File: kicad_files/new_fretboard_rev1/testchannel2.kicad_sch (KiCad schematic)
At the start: 22 parts, among them U2 LX3302AQPW-TR-EASY

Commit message: version with three coil circuits, some errors
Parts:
- removed C12, C13: 680pf, Capacitor_SMD:C_0603_1608Metric, symbol Device:C
- removed C14, C15: 10pf, Capacitor_SMD:C_0402_1005Metric, symbol Device:C
- removed C16: 1uf, Capacitor_SMD:C_0603_1608Metric, symbol Device:C
- removed C17, C20: 100nf, Capacitor_SMD:C_0402_1005Metric, symbol Device:C
- removed C18, C19: 6.8nf, Capacitor_SMD:C_0402_1005Metric, symbol Device:C
- removed C21: 1000pf, Capacitor_SMD:C_0402_1005Metric, symbol Device:C
- removed C22: 470nf, Capacitor_SMD:C_0402_1005Metric, symbol Device:C
- removed L5, L6, L7, L8: L, NetTie:NetTie-2_SMD_Pad0.5mm, symbol Device:L
- removed R10, R11, R8, R9: 10R, Resistor_SMD:R_0402_1005Metric, symbol Device:R
- removed R12: 221R, Resistor_SMD:R_0402_1005Metric, symbol Device:R
- removed R13: 4.7R, Resistor_SMD:R_0402_1005Metric, symbol Device:R
- removed U2: LX3302AQPW-TR-EASY, Snapeda:14-TSSOP_MCH-L, symbol Snapeda:LX3302AQPW-TR-EASY
- added C23, C29: 100nf, Capacitor_SMD:C_0402_1005Metric, symbol Device:C
- added C24: 1000pf, Capacitor_SMD:C_0402_1005Metric, symbol Device:C
- added C25: 470nf, Capacitor_SMD:C_0402_1005Metric, symbol Device:C
- added C26: 1uf, Capacitor_SMD:C_0603_1608Metric, symbol Device:C
- added C27, C28: 6.8nf, Capacitor_SMD:C_0402_1005Metric, symbol Device:C
- added C30, C31: 10pf, Capacitor_SMD:C_0402_1005Metric, symbol Device:C
- added C32, C33: 680pf, Capacitor_SMD:C_0603_1608Metric, symbol Device:C
- added L10, L11, L12, L9: L, NetTie:NetTie-2_SMD_Pad0.5mm, symbol Device:L
- added R14: 221R, Resistor_SMD:R_0402_1005Metric, symbol Device:R
- added R15, R16, R17, R18: 10R, Resistor_SMD:R_0402_1005Metric, symbol Device:R
- added R7: 4.7R, Resistor_SMD:R_0402_1005Metric, symbol Device:R
- added U3: LX3302AQPW-TR-EASY, Snapeda:14-TSSOP_MCH-L, symbol Snapeda:LX3302AQPW-TR-EASY
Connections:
- net CL1B_A: now also L12.1, R18.2
- net CL1_A: now also C30.1, R18.1, U3.8 (CL1)
- net CL2B_A: now also L11.1, R17.2
- net CL2_A: now also C31.1, R17.1, U3.10 (CL2)
- net GND: now also C23.1, C24.1, C25.1, C26.1, C27.1, C28.1, C30.2, C31.2, C32.2, C33.2, L11.2, L12.2, U3.2 (GND), U3.9 (GNDCL)
- net OSC11_A: now also C32.1, L9.2, U3.13 (OSC1)
- net OSC12_A: now also C33.1, L10.2, U3.12 (OSC2)
- net SUB_A: now also C29.1, U3.11 (SUB)
- net VIN_A: now also C24.2, C25.2, R15.2, R16.1, R7.1, U3.4 (VIN)
- new net: C26.2, C29.2, U3.5 (VDD)
- new net: C23.2, R7.2
- new net: C28.2, R14.1, R15.1, U3.6 (IO2)
- new net: C27.2, R14.2
- new net /OSC2B_A: L10.1, L9.1, R16.2
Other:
- removed sheet testchannel1
- removed sheet testchannel2

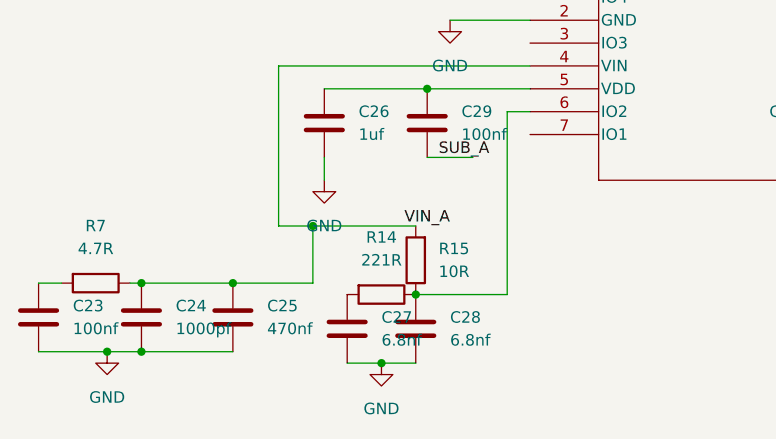
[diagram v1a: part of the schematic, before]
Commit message: stm32 micro added
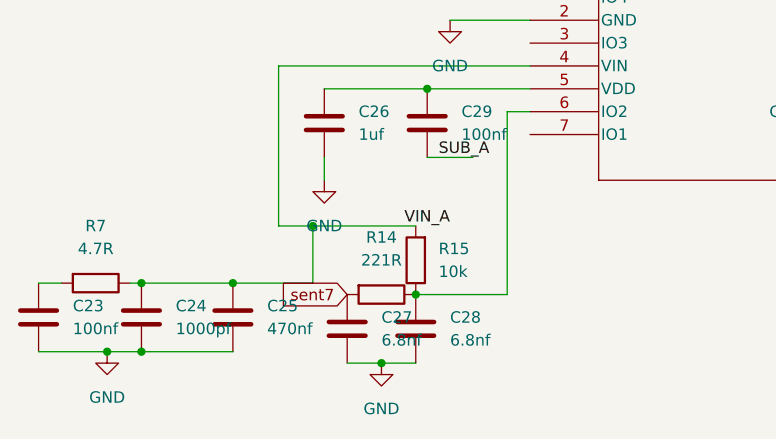
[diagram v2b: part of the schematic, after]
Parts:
- R15: value 10R -> 10k
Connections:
- net sent7: now reaches C27.2, R14.2

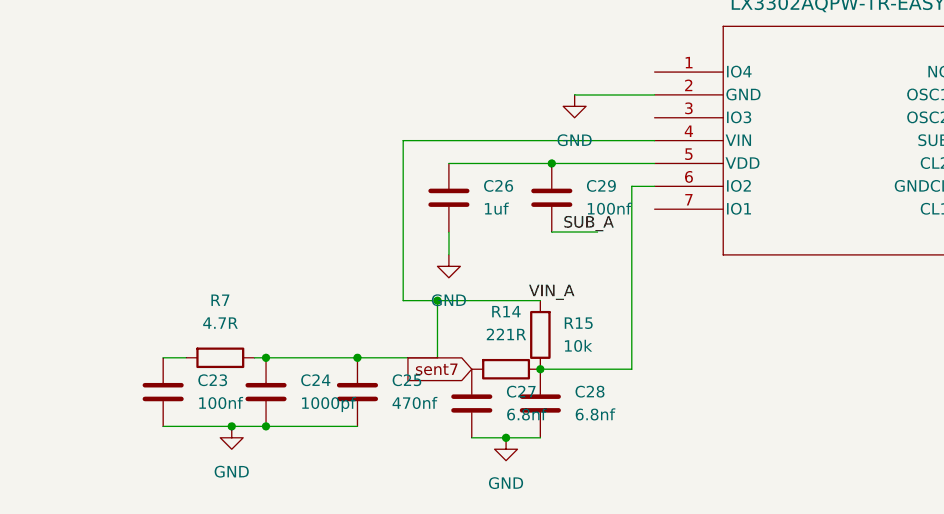
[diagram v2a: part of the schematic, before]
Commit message: mcu configured, still needs power connections and spi i2c connections
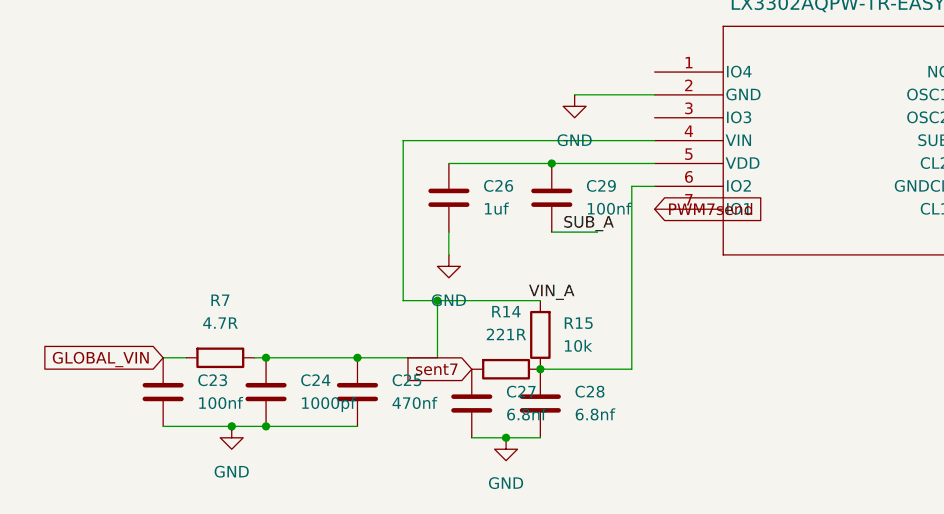
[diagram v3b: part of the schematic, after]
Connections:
- net GLOBAL_VIN: now reaches C23.2, R7.2
- net PWM7send: now reaches U3.7 (IO1)
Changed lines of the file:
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@@
+		)
+	)
+	(global_label "PWM7send"
+		(shape input)
+		(at 97.79 102.87 0)
+		(fields_autoplaced yes)
+		(effects
+			(font
+				(size 1.27 1.27)
+			)
+			(justify left)
+		)
+		(property "Intersheetrefs" "${INTERSHEET_REFS}"
+			(at 110.5722 102.87 0)
+			(effects
+				(font
+					(size 1.27 1.27)
+				)
+				(justify left)
+				(hide yes)
+			)
+		)
+	)
+	(global_label "GLOBAL_VIN"
+		(shape input)
+		(at 43.18 119.38 180)
+		(fields_autoplaced yes)
+		(effects
+			(font
+				(size 1.27 1.27)
+			)
+			(justify right)
+		)
+		(property "Intersheetrefs" "${INTERSHEET_REFS}"
+			(at 29.188 119.38 0)
+			(effects
+				(font
+					(size 1.27 1.27)
+				)
+				(justify right)
+				(hide yes)
+			)
 		)
 	)

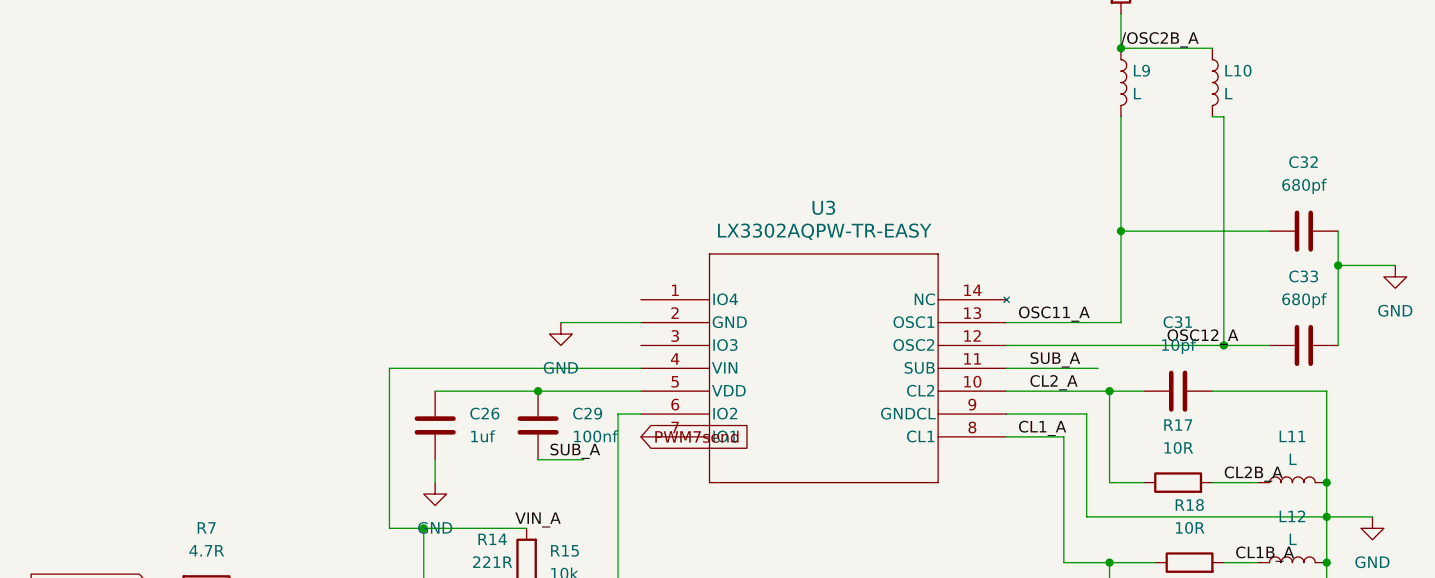
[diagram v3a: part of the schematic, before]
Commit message: finished routing - adding silkscreen
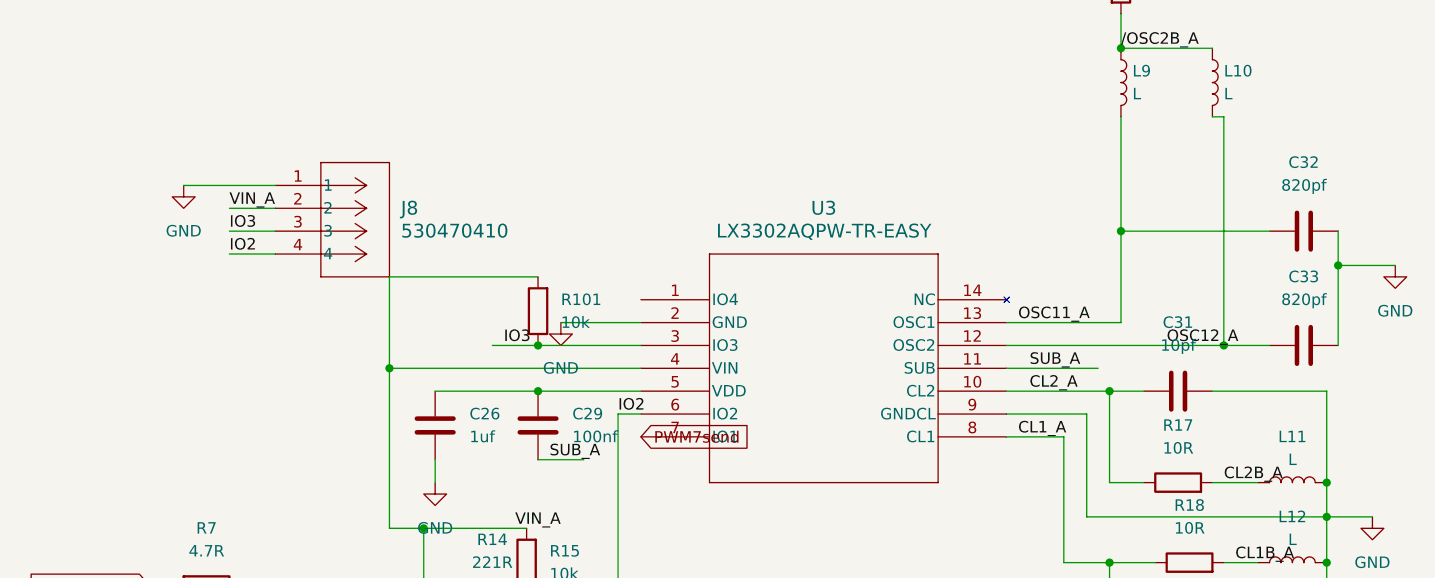
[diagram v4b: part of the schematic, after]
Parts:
- added J8: 530470410, Snapeda:CONN04_530470410_MOL, symbol Snapeda:530470410
- added R101: 10k, Resistor_SMD:R_0402_1005Metric, symbol Device:R
- C32, C33: value 680pf -> 820pf
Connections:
- net GND: now also J8.1
- net VIN_A: now also J8.2, R101.2
- net IO3: now reaches U3.3 (IO3)
- net IO3: now also J8.3, R101.1
- net IO2: now reaches C28.2, R14.1, R15.1, U3.6 (IO2)
- net IO2: now also J8.4

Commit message: exported gerbers of lefthand
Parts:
- L10, L11, L12, L9: now left out of the parts list
